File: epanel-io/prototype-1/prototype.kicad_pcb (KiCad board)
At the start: 2 copper layers, 28 parts, among them J1 Conn_01x05_Male, J2 Screw_Terminal_01x02, J3 Screw_Terminal_01x02, J4 Screw_Terminal_01x02, Q1 IRF830, Q2 BT136-600, U1 4N35, U2 H11AA1, U3 MOC3021M

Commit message: first draft
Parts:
- moved J1 45.7 mm to (101.6, 71.1)
- moved R8 35.7 mm to (109.2, 88.9), turned to -90 degrees
- moved R12 33.1 mm to (109.2, 76.2), turned to -90 degrees
- moved R6 32.5 mm to (162.6, 101.6), turned to 180 degrees
- moved R7 32.5 mm to (162.6, 96.5), turned to 180 degrees
- moved R1 30.6 mm to (109.2, 63.5), turned to -90 degrees
- moved U1 29.7 mm to (119.4, 66.0)
- moved U2 29.7 mm to (119.4, 91.4)
- moved U3 29.0 mm to (119.4, 78.7)
- moved C4 20.9 mm to (142.2, 81.3)
- moved R3 19.3 mm to (119.4, 48.3)
- moved R10 18.5 mm to (142.2, 76.2), turned to -90 degrees
- moved Q2 18.5 mm to (160.0, 78.7)
- moved R11 18.5 mm to (137.2, 76.2), turned to 90 degrees
- moved R4 17.0 mm to (124.5, 48.3)
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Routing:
- net GND: track 0.00 -> 68.4 mm
- net Net-(C1-Pad2): track 0.00 -> 53.5 mm, vias 0 -> 2
- net Net-(Q2-Pad3): track 0.00 -> 51.3 mm, vias 0 -> 2
- net Net-(C3-Pad2): track 0.00 -> 40.8 mm
- net Net-(R6-Pad2): track 0.00 -> 39.6 mm
- net Net-(R7-Pad2): track 0.00 -> 38.6 mm
- net Net-(Q2-Pad2): track 0.00 -> 35.3 mm
- net Net-(C1-Pad1): track 0.00 -> 34.4 mm
- net Net-(D2-Pad1): track 0.00 -> 33.0 mm
- net +3V3: track 0.00 -> 26.2 mm
- net Net-(Q1-Pad1): track 0.00 -> 25.5 mm
- net Net-(J1-Pad3): track 0.00 -> 18.0 mm
- net Net-(J1-Pad5): track 0.00 -> 17.3 mm
- net Net-(R11-Pad2): track 0.00 -> 14.2 mm
- net Net-(J3-Pad2): track 0.00 -> 11.8 mm
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
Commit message: fixes
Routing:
- net Net-(Q2-Pad3): track 51.3 -> 50.0 mm
- net Net-(R7-Pad2): track 38.6 -> 39.4 mm
- net Net-(R6-Pad2): track 39.6 -> 40.5 mm
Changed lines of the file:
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@@
   (segment (start 101.6 71.12) (end 99.06 73.66) (width 0.25) (layer "F.Cu") (net 9))
   (arc (start 104.14 88.9) (mid 105.053811 89.51059) (end 106.131726 89.725) (width 0.25) (layer "F.Cu") (net 9))
-  (segment (start 119.38 78.74) (end 119.38 71.12) (width 0.25) (layer "F.Cu") (net 10))
   (segment (start 104.14 73.66) (end 101.6 73.66) (width 0.25) (layer "F.Cu") (net 10))
-  (segment (start 115.57 78.74) (end 116.84 78.74) (width 0.25) (layer "F.Cu") (net 10))
+  (segment (start 115.57 78.74) (end 119.38 78.74) (width 0.25) (layer "F.Cu") (net 10))
   (segment (start 119.38 63.5) (end 114.3 58.42) (width 0.25) (layer "F.Cu") (net 10))
   (segment (start 115.57 66.04) (end 119.38 66.04) (width 0.25) (layer "F.Cu") (net 10))
@@
   (segment (start 114.615 88.9) (end 116.84 88.9) (width 0.25) (layer "F.Cu") (net 10))
   (segment (start 114.3 58.42) (end 109.22 58.42) (width 0.25) (layer "F.Cu") (net 10))
-  (segment (start 116.84 78.74) (end 119.38 78.74) (width 0.25) (layer "F.Cu") (net 10))
   (segment (start 119.38 66.04) (end 119.38 63.5) (width 0.25) (layer "F.Cu") (net 10))
-  (segment (start 119.38 66.04) (end 119.38 71.12) (width 0.25) (layer "F.Cu") (net 10))
+  (segment (start 119.38 66.04) (end 119.38 78.74) (width 0.25) (layer "F.Cu") (net 10))
   (segment (start 119.38 86.36) (end 119.38 78.74) (width 0.25) (layer "F.Cu") (net 10))
   (segment (start 109.22 58.42) (end 106.68 60.96) (width 0.25) (layer "F.Cu") (net 10))
@@
   (segment (start 132.08 78.74) (end 129.54 81.28) (width 0.25) (layer "F.Cu") (net 17))
   (segment (start 164.472305 76.46) (end 164.22 76.46) (width 0.25) (layer "F.Cu") (net 17))
-  (segment (start 123.19 81.28) (end 121.92 81.28) (width 0.25) (layer "F.Cu") (net 17))
   (segment (start 162.56 73.66) (end 132.08 73.66) (width 0.25) (layer "F.Cu") (net 17))
   (segment (start 129.54 81.28) (end 123.19 81.28) (width 0.25) (layer "F.Cu") (net 17))
@@
   (arc (start 111.211726 63.5) (mid 110.133812 63.28559) (end 109.22 62.675) (width 0.25) (layer "F.Cu") (net 18))
   (segment (start 120.205 48.26) (end 123.635 48.26) (width 0.25) (layer "F.Cu") (net 19))
-  (segment (start 160.02 101.6) (end 154.94 96.52) (width 0.25) (layer "F.Cu") (net 20))
-  (segment (start 161.6475 101.6) (end 160.02 101.6) (width 0.25) (layer "F.Cu") (net 20))
-  (segment (start 154.94 96.52) (end 124.145 96.52) (width 0.25) (layer "F.Cu") (net 20))
-  (segment (start 161.6475 96.52) (end 160.02 96.52) (width 0.25) (layer "F.Cu") (net 21))
-  (segment (start 157.48 93.98) (end 124.145 93.98) (width 0.25) (layer "F.Cu") (net 21))
-  (segment (start 160.02 96.52) (end 157.48 93.98) (width 0.25) (layer "F.Cu") (net 21))
+  (segment (start 152.4 93.98) (end 158.869183 100.449184) (width 0.25) (layer "F.Cu") (net 20))
+  (segment (start 152.4 93.98) (end 124.145 93.98) (width 0.25) (layer "F.Cu") (net 20))
+  (arc (start 161.6475 101.6) (mid 160.143886 101.300913) (end 158.869183 100.449184) (width 0.25) (layer "F.Cu") (net 20))
+  (segment (start 158.869183 95.369184) (end 154.94 91.44) (width 0.25) (layer "F.Cu") (net 21))
+  (segment (start 154.94 91.44) (end 124.145 91.44) (width 0.25) (layer "F.Cu") (net 21))
+  (arc (start 161.6475 96.52) (mid 160.143886 96.220913) (end 158.869183 95.369184) (width 0.25) (layer "F.Cu") (net 21))
   (segment (start 135.168274 76.2) (end 123.19 76.2) (width 0.25) (layer "F.Cu") (net 22))
   (arc (start 137.16 75.375) (mid 136.246188 75.985589) (end 135.168274 76.2) (width 0.25) (layer "F.Cu") (net 22))
@@
   (segment (start 175.25 60.97) (end 175.26 60.96) (width 0.25) (layer "F.Cu") (net 30))
   (segment (start 164.39 60.97) (end 175.25 60.97) (width 1) (layer "F.Cu") (net 30))
-  (segment (start 164.4 60.96) (end 164.39 60.97) (width 0.25) (layer "F.Cu") (net 30))
   (segment (start 175.25 55.87) (end 175.26 55.88) (width 0.25) (layer "F.Cu") (net 31))
-  (segment (start 164.4 55.88) (end 164.39 55.87) (width 0.25) (layer "F.Cu") (net 31))
   (segment (start 164.39 55.87) (end 175.25 55.87) (width 1) (layer "F.Cu") (net 31))
   (segment (start 164.22 78.74) (end 167.64 78.74) (width 1) (layer "F.Cu") (net 32))

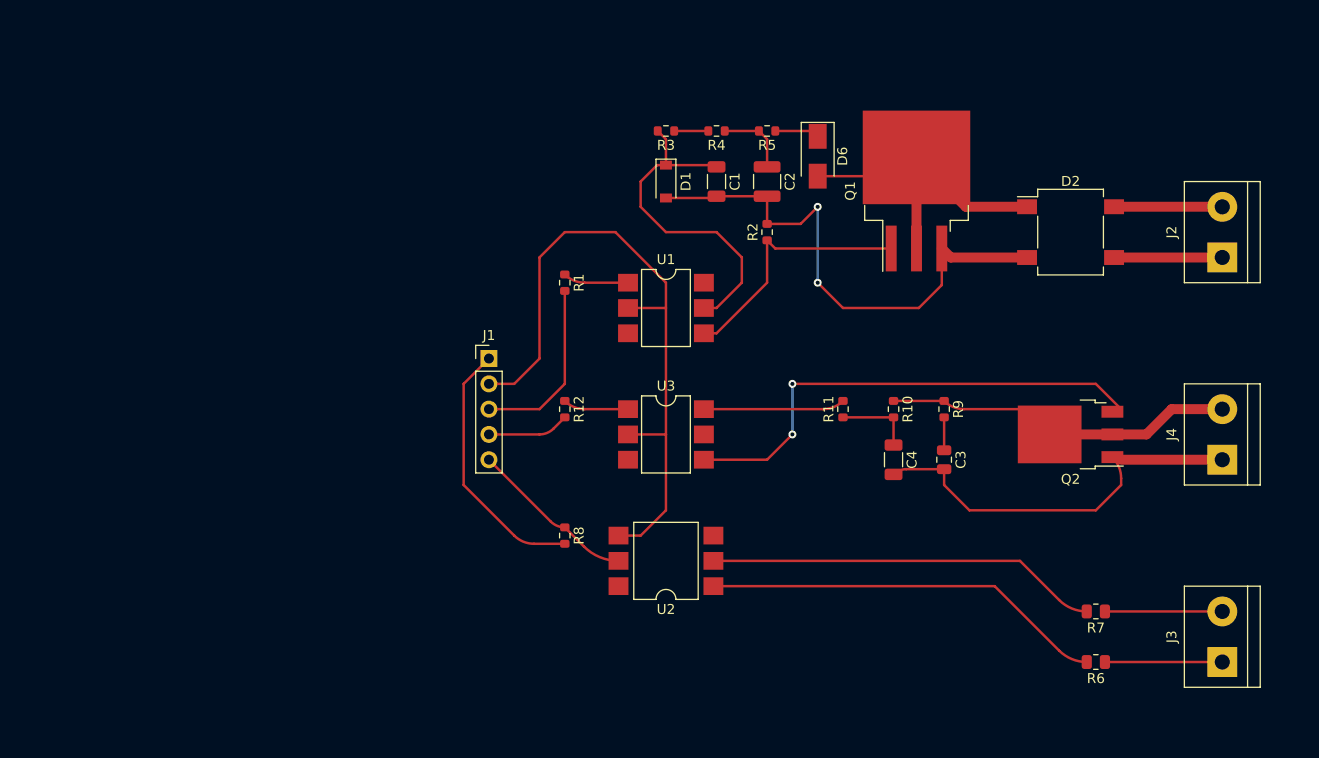
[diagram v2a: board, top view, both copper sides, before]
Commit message: board outline (DRC ok)
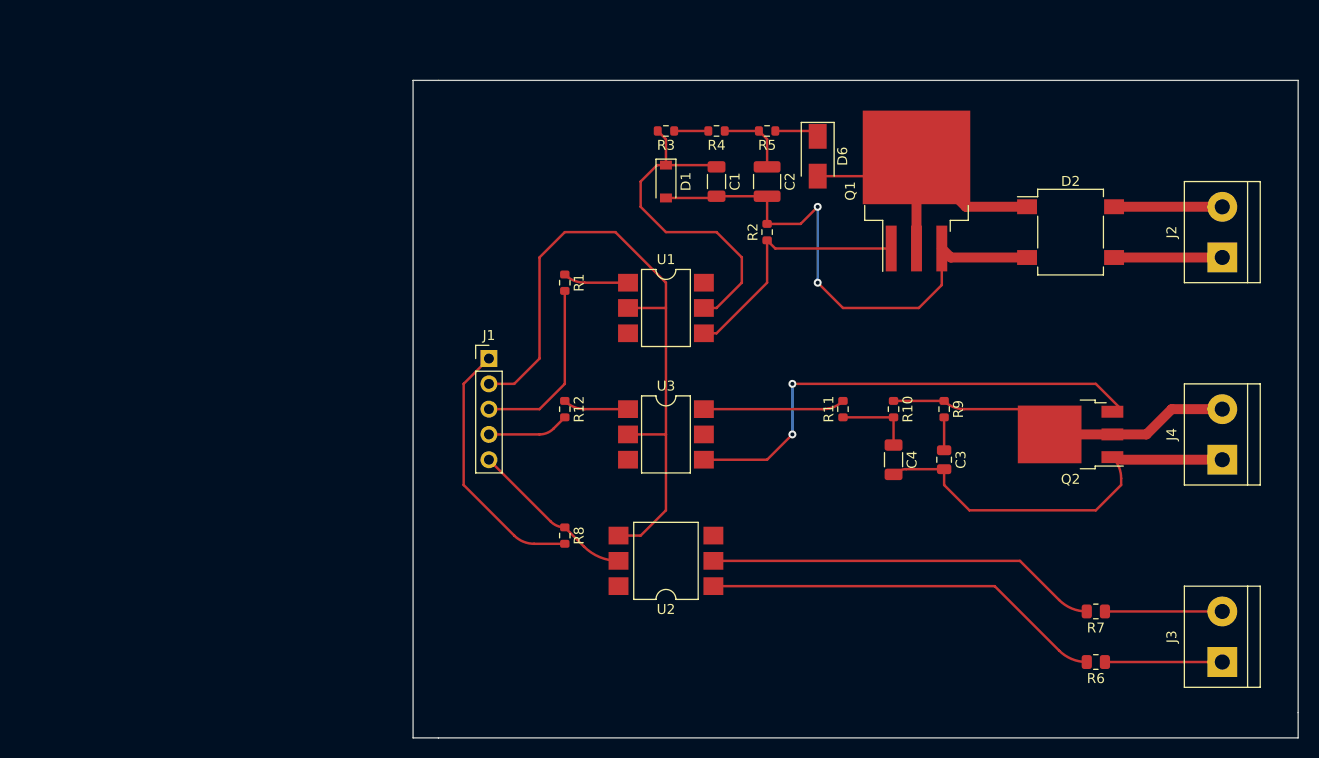
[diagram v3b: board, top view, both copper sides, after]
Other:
- board outline added: 88.9 x 66 mm
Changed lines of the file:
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@@
     )
   )
+  (gr_line (start 182.88 43.18) (end 182.88 106.68) (layer "Edge.Cuts") (width 0.1))
+  (gr_line (start 182.88 109.22) (end 96.52 109.22) (layer "Edge.Cuts") (width 0.1))
+  (gr_line (start 96.52 43.18) (end 182.88 43.18) (layer "Edge.Cuts") (width 0.1))
+  (gr_line (start 96.52 109.22) (end 93.98 109.22) (layer "Edge.Cuts") (width 0.1))
+  (gr_line (start 93.98 43.18) (end 96.52 43.18) (layer "Edge.Cuts") (width 0.1))
+  (gr_line (start 93.98 109.22) (end 93.98 43.18) (layer "Edge.Cuts") (width 0.1))
+  (gr_line (start 182.88 106.68) (end 182.88 109.22) (layer "Edge.Cuts") (width 0.1))
   (segment (start 119.38 51.69) (end 118.49 51.69) (width 0.25) (layer "F.Cu") (net 1))
   (segment (start 124.285 51.69) (end 124.46 51.865) (width 0.25) (layer "F.Cu") (net 1))
